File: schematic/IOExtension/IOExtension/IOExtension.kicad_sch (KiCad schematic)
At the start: 32 parts, among them J1 Address, J10 Opto_GPB2, J11 Opto_GPB3, J12 IO_GPB, J13 Opto_GPB4, J14 OLED_SCR, J2 TTL Serial OUT, J3 PORT_C_IN, J4 PORT_C_OUT, J5 INTs/Ts, J6 TTL Serial IN, J7 INTs/Ts, J8 IO_GPA, J9 Opto_IN, U1 MCP23017_SP, U2 4N25, U3 4N25, U4 4N25

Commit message: Latest shcematic of IOExtesion board and latest Gerbers
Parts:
- added R12, R13: 1K, Resistor_THT:R_Axial_DIN0204_L3.6mm_D1.6mm_P7.62mm_Horizontal, symbol Device:R
- added SW1: B_USER1, Button_Switch_THT:SW_PUSH_6mm_H5mm, symbol Switch:SW_Push
- added U5: 24LC512, Package_DIP:DIP-8_W7.62mm, symbol Memory_EEPROM:24LC512
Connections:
- net +5V: now also R12.2, R13.2, U5.3 (A2), U5.8 (VCC)
- net GND: now also SW1.1, U5.1 (A0), U5.2 (A1), U5.4 (GND), U5.7 (WP)
- net SCK: now also R13.1, U5.6 (SCL)
- net SDA: now also R12.1, U5.5 (SDA)
- net at J8.1 (Pin_1), U1.28 (GPA7): now also SW1.2

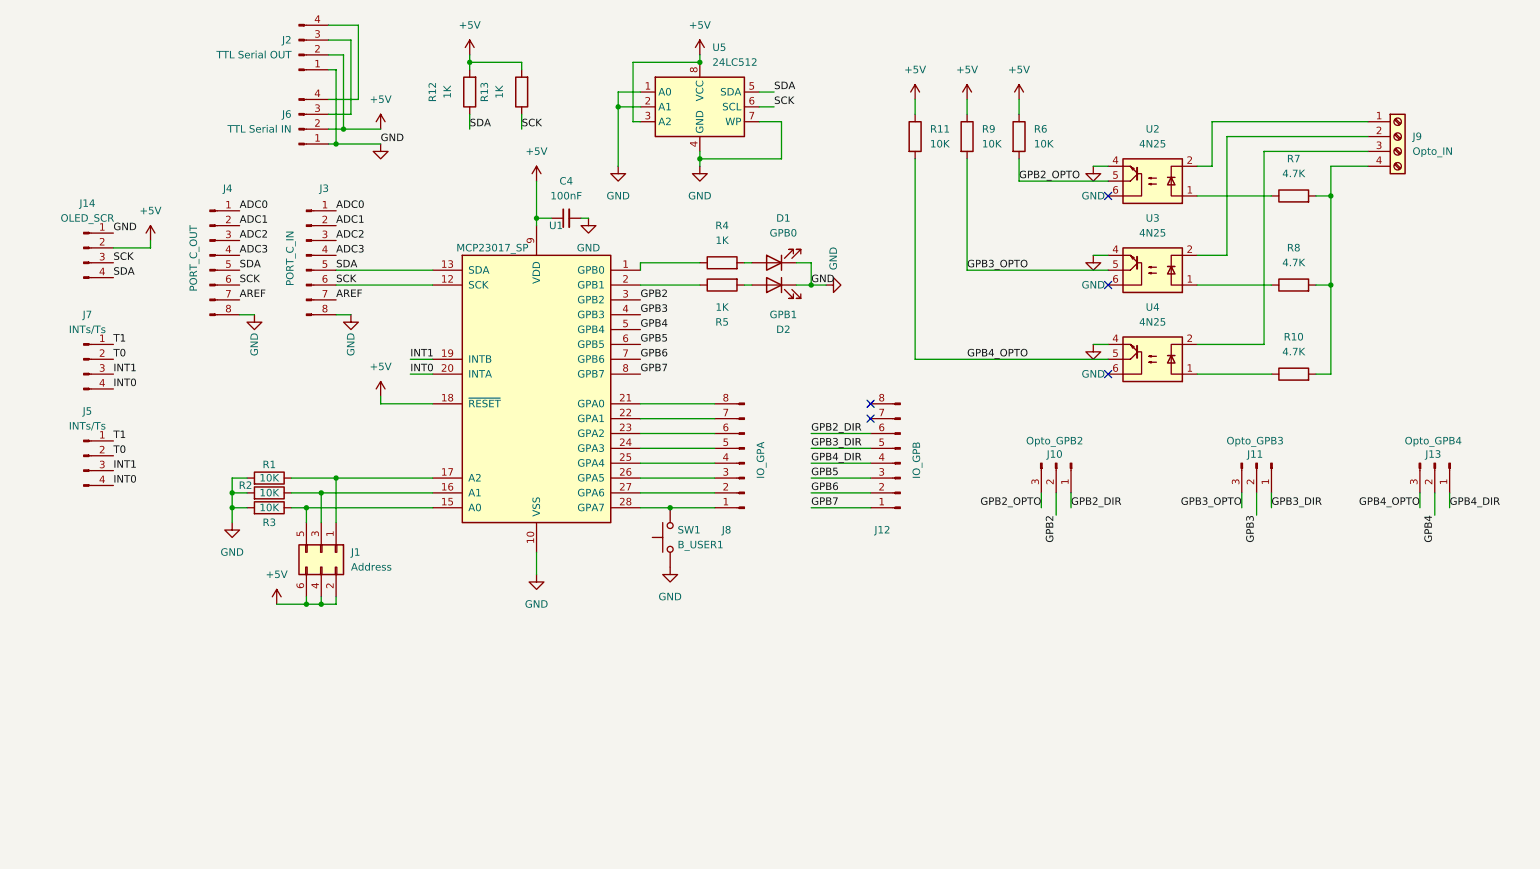
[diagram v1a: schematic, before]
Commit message: Latest schematic of IOExtension modifications
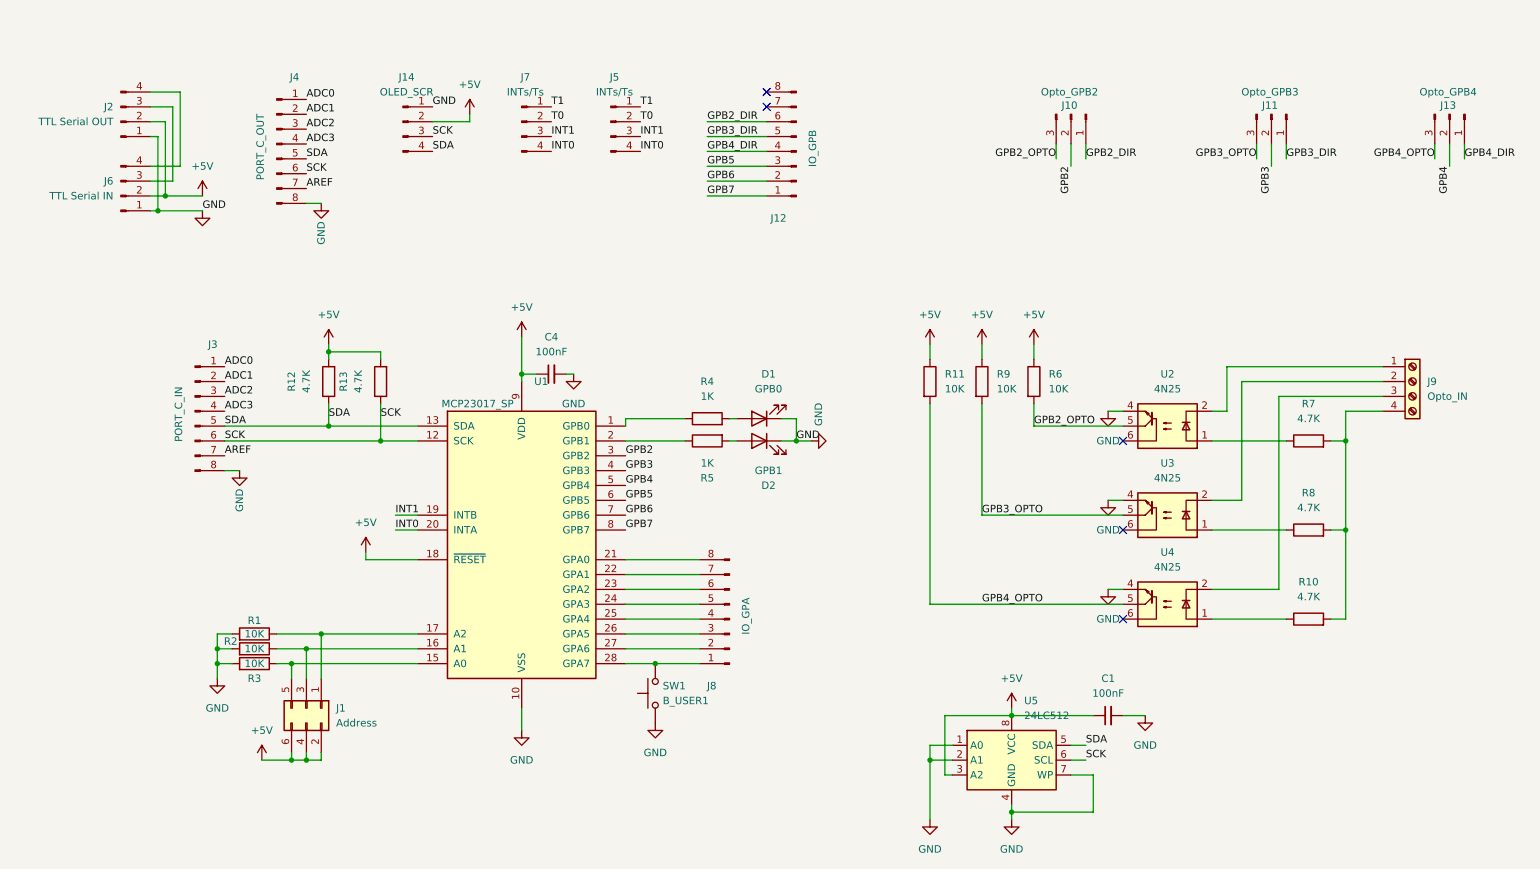
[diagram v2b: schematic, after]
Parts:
- added C1: 100nF, Capacitor_THT:C_Disc_D7.0mm_W2.5mm_P5.00mm, symbol Device:C_Small
- R12, R13: value 1K -> 4.7K
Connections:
- net +5V: now also C1.1
- net GND: now also C1.2
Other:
- moved on the sheet: C4, D1, D2, J1, J10, J11, J12, J13, J14, J2, J3, J4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
